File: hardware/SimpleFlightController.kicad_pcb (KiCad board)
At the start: 2 copper layers, 40 x 46 mm, 79 parts, among them J1 Screw_Terminal_01x02, J2 Conn_01x03, J3 Conn_01x03, U1 BQ25883RGER, U2 ICM-45686, U3 STM32F722RETx, U4 BMP580, U5 TPS63070RNMR, U6 LMR51430, X1 X322525MOB4SI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

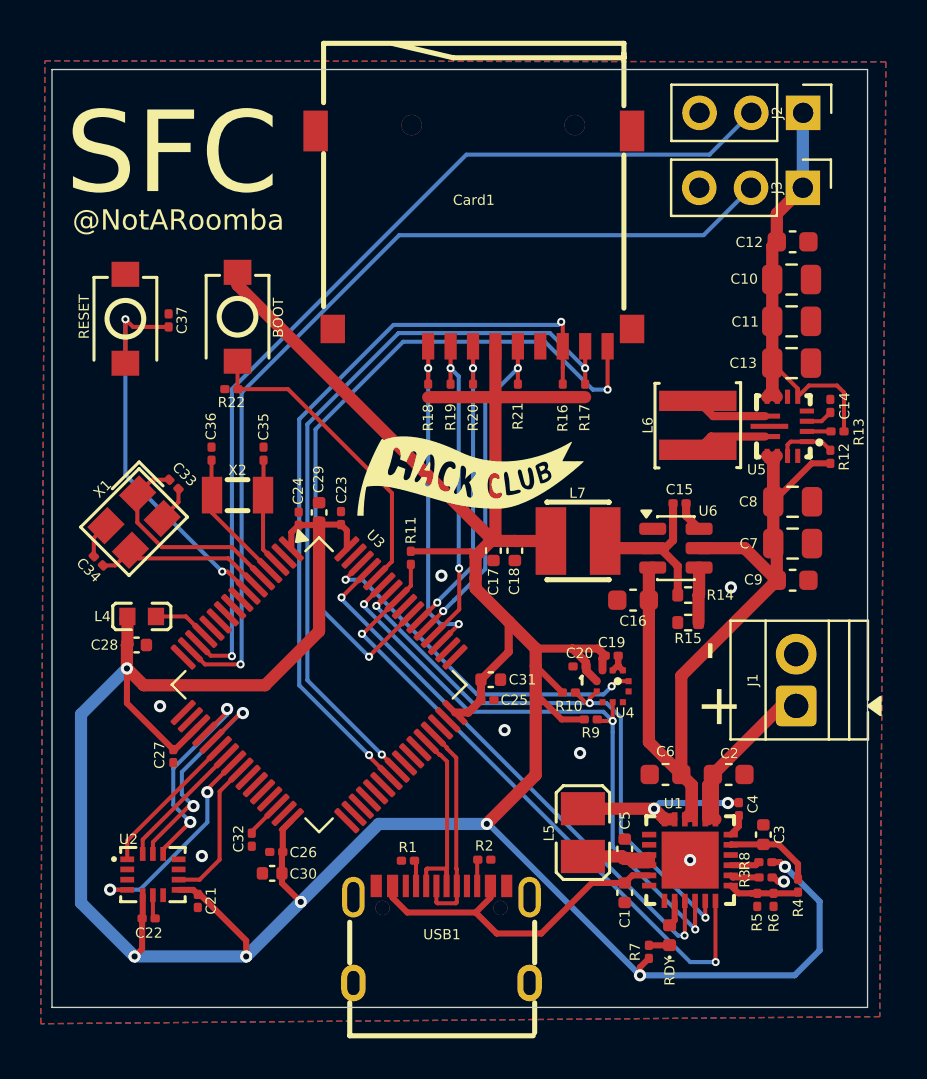
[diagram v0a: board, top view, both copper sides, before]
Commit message: flip led
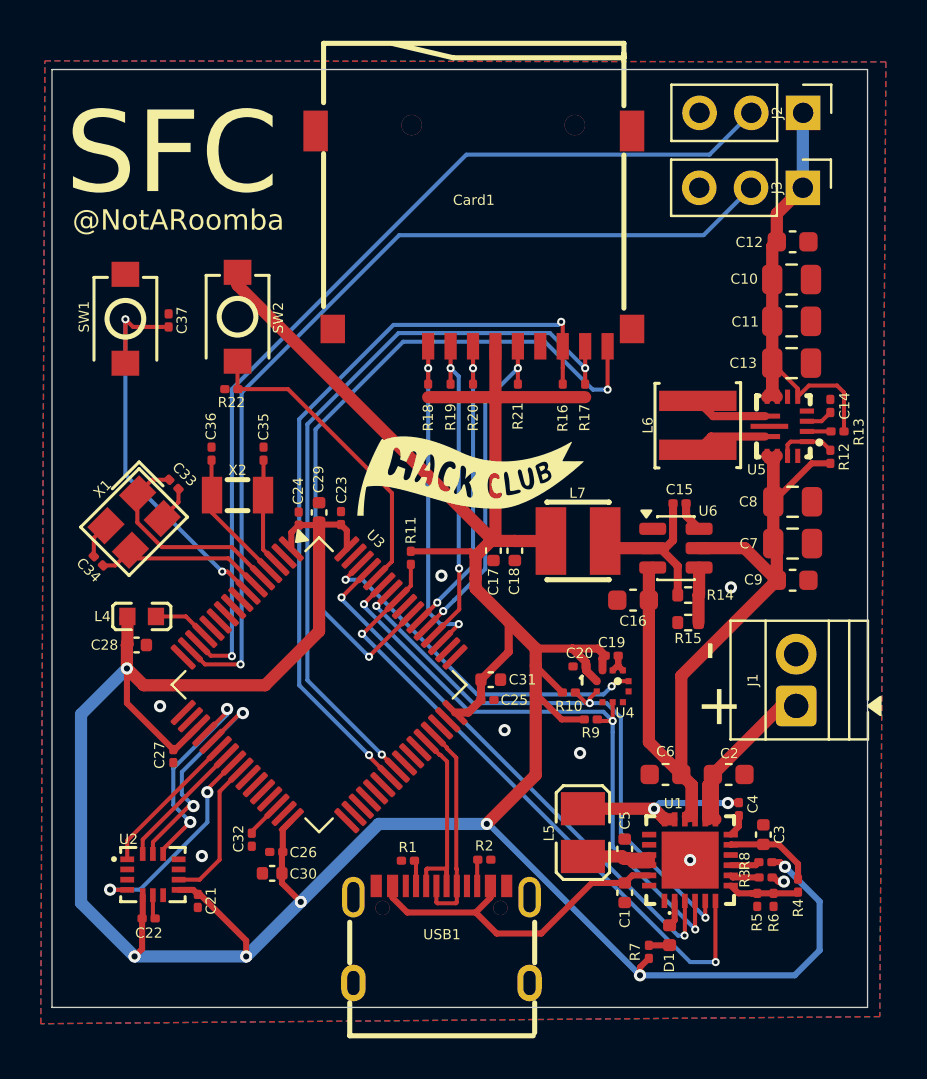
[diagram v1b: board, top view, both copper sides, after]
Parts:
- turned D1 to -90 degrees
- renumbered RDY to D1, RESET to SW1, BOOT to SW2
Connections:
- R7 pad 1: Net-(D1-K) -> Net-(D1-A)
- U1 pad 2: Net-(D1-A) -> Net-(D1-K)
